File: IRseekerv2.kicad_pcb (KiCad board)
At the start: 2 copper layers, 100 x 100 mm, 39 parts, among them J1 Conn_01x01_Female, J10 Conn_01x01_Female, J11 Conn_01x01_Female, J12 Conn_01x01_Female, J13 RESET, J14 COMM, J15 SEL_VOLTAGE, J16 G, J17 G, J18 G, J19 G, J2 Conn_01x01_Female, J20 COMM, J21 Conn_01x01_Female, J22 Conn_01x01_Female, J23 Conn_01x01_Female, J24 Conn_01x01_Female, J3 Conn_01x01_Female, J4 Conn_01x01_Female, J5 Conn_01x01_Female, J6 Conn_01x01_Female, J7 Conn_01x01_Female, J8 Conn_01x01_Female, J9 Conn_01x01_Female, U1 WeAct-STM32G431CoreBoard, U10 TSSP58038, U11 TSSP58038, U12 TSSP58038, U13 TSSP58038, U14 TSSP58038, U15 TSSP58038, U16 TSSP58038, U2 CD4072B, U4 CD4072B, U5 TSSP58038, U6 TSSP58038, U7 TSSP58038, U8 TSSP58038, U9 TSSP58038

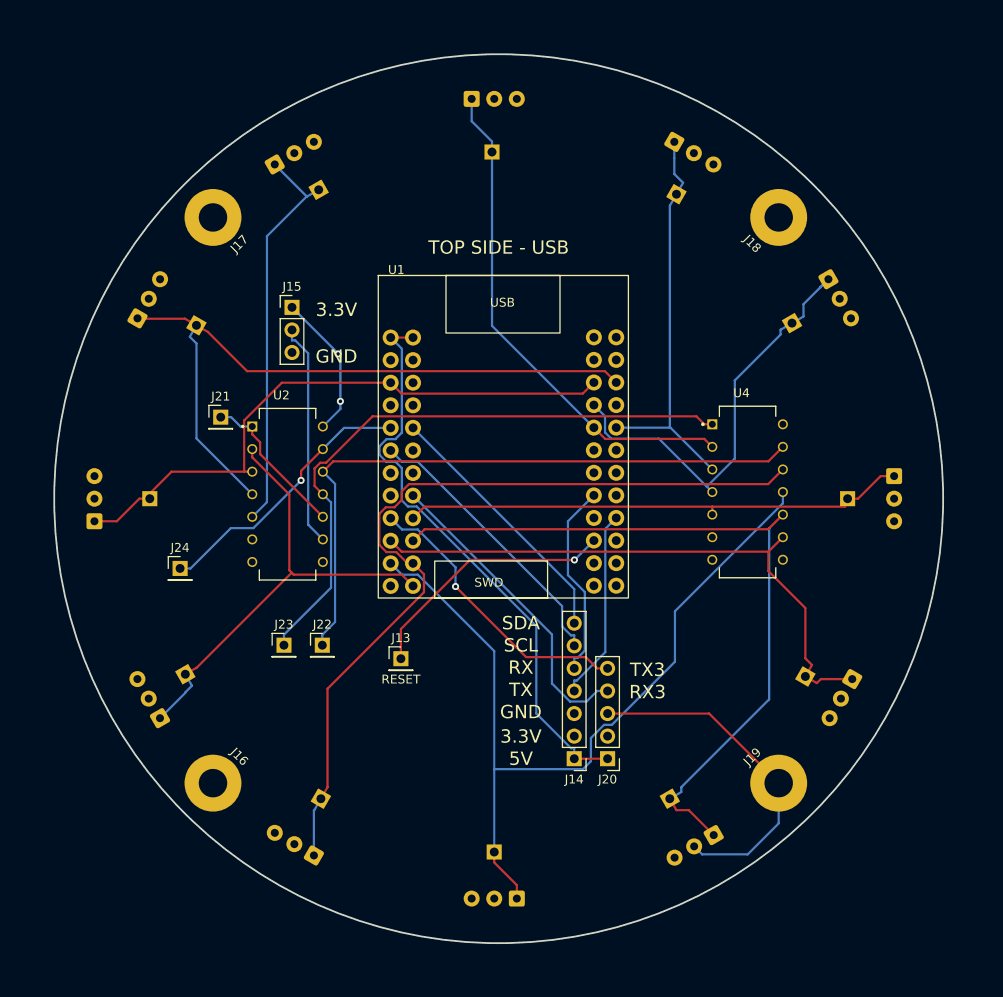
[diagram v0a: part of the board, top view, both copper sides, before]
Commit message: reworked to put STM32G431CBU6 on board
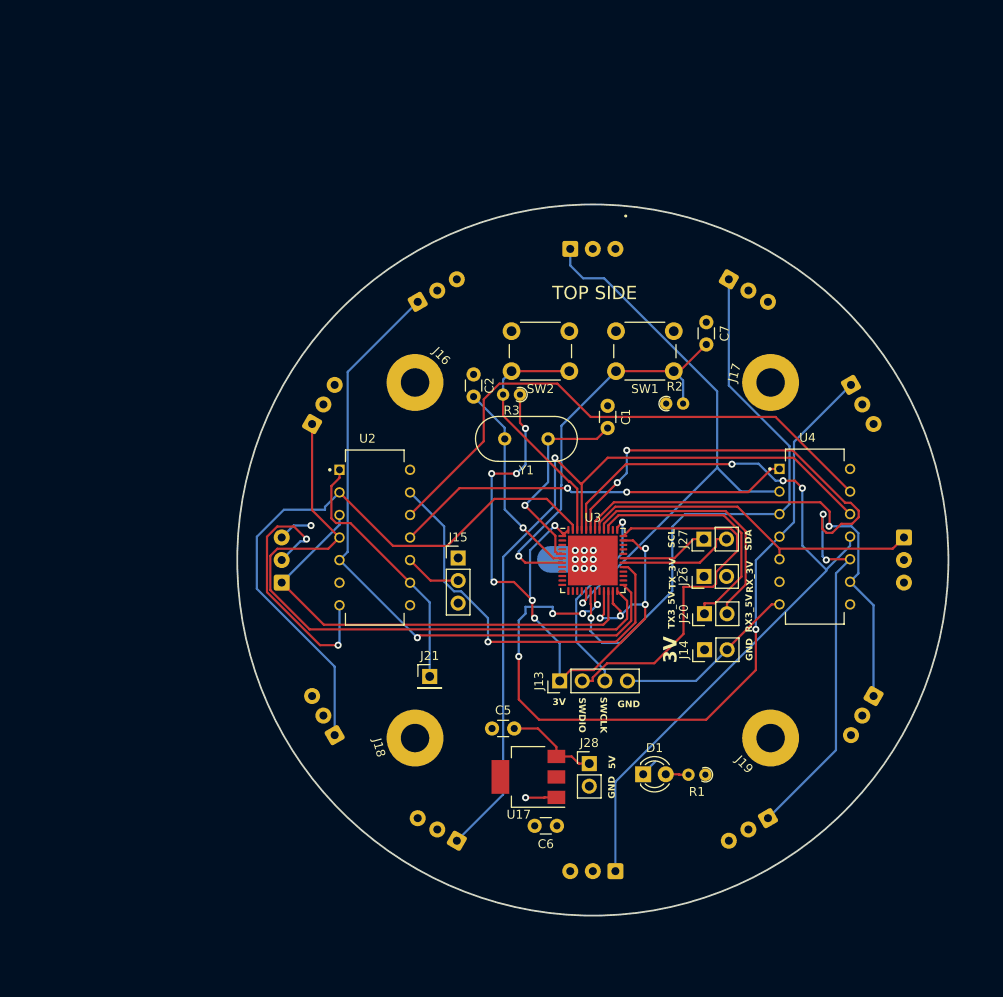
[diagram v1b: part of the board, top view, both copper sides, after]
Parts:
- removed J1, J10, J11, J12, J2, J22, J23, J24, J3, J4, J5, J6, J7, J8, J9: Conn_01x01_Female, Connector_PinHeader_2.54mm:PinHeader_1x01_P2.54mm_Vertical
- removed U1: WeAct-STM32G431CoreBoard, bluepill:WeAct-STM32G431CoreBoard_MCU_Module
- added C1: 10pF, Capacitor_THT:C_Disc_D3.0mm_W1.6mm_P2.50mm, F.Cu at (105.8, 83.1)
- added C2: 10pF, Capacitor_THT:C_Disc_D3.0mm_W1.6mm_P2.50mm, F.Cu at (90.7, 79.5)
- added C5: 10uF, Capacitor_THT:C_Disc_D3.0mm_W1.6mm_P2.50mm, F.Cu at (92.8, 119.3)
- added C6: 10uF, Capacitor_THT:C_Disc_D3.0mm_W1.6mm_P2.50mm, F.Cu at (100.0, 130.3)
- added C7: 100nF, Capacitor_THT:C_Disc_D3.0mm_W1.6mm_P2.50mm, F.Cu at (116.9, 73.7)
- added D1: LED, LED_THT:LED_D3.0mm, F.Cu at (109.8, 124.5)
- added J26: Conn_01x02_Pin, Connector_PinHeader_2.54mm:PinHeader_1x02_P2.54mm_Vertical, F.Cu at (116.6, 102.2)
- added J27: Conn_01x02_Pin, Connector_PinHeader_2.54mm:PinHeader_1x02_P2.54mm_Vertical, F.Cu at (116.6, 98.0)
- added J28: Conn_01x02_Pin, Connector_PinHeader_2.54mm:PinHeader_1x02_P2.54mm_Vertical, F.Cu at (103.7, 123.3)
- added R1: 330R, Resistor_THT:R_Axial_DIN0204_L3.6mm_D1.6mm_P1.90mm_Vertical, F.Cu at (116.8, 124.5)
- added R2: 10kR, Resistor_THT:R_Axial_DIN0204_L3.6mm_D1.6mm_P1.90mm_Vertical, F.Cu at (112.3, 82.8)
- added R3: 10kR, Resistor_THT:R_Axial_DIN0204_L3.6mm_D1.6mm_P1.90mm_Vertical, F.Cu at (95.9, 81.8)
- added SW1: SW_Push, Button_Switch_THT:SW_PUSH_6mm, F.Cu at (113.2, 79.2)
- added SW2: SW_Push, Button_Switch_THT:SW_PUSH_6mm, F.Cu at (101.4, 79.2)
- added U17: AMS1117-3.3, Package_TO_SOT_SMD:SOT-223-3_TabPin2, F.Cu at (96.8, 124.8)
- added U3: STM32G431CBUx, Package_DFN_QFN:QFN-48-1EP_7x7mm_P0.5mm_EP5.6x5.6mm, F.Cu at (104.1, 100.5)
- added Y1: Crystal, Crystal:Crystal_HC49-4H_Vertical, F.Cu at (99.1, 86.8)
- J13: value RESET -> Conn_01x04_Pin; footprint Connector_PinHeader_2.54mm:PinHeader_1x01_P2.54mm_Vertical -> Connector_PinHeader_2.54mm:PinHeader_1x04_P2.54mm_Vertical
- J14: value COMM -> Conn_01x02_Pin; footprint Connector_PinHeader_2.54mm:PinHeader_1x07_P2.54mm_Vertical -> Connector_PinHeader_2.54mm:PinHeader_1x02_P2.54mm_Vertical
- J20: value COMM -> Conn_01x02_Pin; footprint Connector_PinHeader_2.54mm:PinHeader_1x05_P2.54mm_Vertical -> Connector_PinHeader_2.54mm:PinHeader_1x02_P2.54mm_Vertical
- U10, U12, U14, U15, U5, U7: value TSSP58038 -> TSSP4038; footprint OptoDevice:Vishay_MINICAST-3Pin -> Vishay:Vishay_MINICAST-3Pin
- U11, U13, U16, U6, U8, U9: value TSSP58038 -> TSSP4038; footprint Library:Vishay_MINICAST-3PinMarek -> Vishay:Vishay_MINICAST-3Pin
- U2: value CD4072B -> CD4012; footprint CD4072B:DIP794W45P254L1969H508Q14 -> CD70xx:DIP794W45P254L1969H508Q14
- U4: value CD4072B -> CD4012B; footprint CD4072B:DIP794W45P254L1969H508Q14 -> CD70xx:DIP794W45P254L1969H508Q14
- moved J18 71.4 mm to (84.1, 120.4), turned to 105 degrees
- moved J17 65.4 mm to (124.1, 80.4), turned to 75 degrees
- moved J16 50.5 mm to (84.1, 80.4)
- moved J21 37.5 mm to (85.7, 113.5)
- moved J15 33.8 mm to (88.9, 100.2)
- moved U16 23.3 mm to (86.6, 70.1)
- moved U15 23.0 mm to (73.8, 82.9)
- moved U5 21.7 mm to (104.1, 65.4)
- moved U14 21.5 mm to (69.1, 100.4)
- moved U13 20.6 mm to (73.8, 117.9)
- moved J20 19.6 mm to (116.6, 106.4), turned to 90 degrees
- moved J14 19.1 mm to (116.7, 110.5), turned to 90 degrees
- moved J13 18.0 mm to (100.4, 114.0), turned to 90 degrees
- moved U6 17.3 mm to (121.6, 70.1)
- moved U7 14.6 mm to (134.4, 82.9)
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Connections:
- J13 pad 1: Net-(J13-Pad1) -> +3.3V
- J14 pad 1: +5V -> +3.3V
- J14 pad 2: +3.3V -> GND
- J15 pad 2: Net-(J15-Pad2) -> Net-(J15-Pin_2)
- J20 pad 1: +5V -> TX3_5V
- J20 pad 2: +3.3V -> RX3_5V
- J21 pad 1: Net-(U2-PadP1) -> Net-(J21-Pin_1)
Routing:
- net +3.3V: track 16.5 -> 91.9 mm, vias 2 -> 12
- net Net-(U2-PadP12): track 73.6 -> 0.00 mm
- net Net-(U2-PadP11): track 70.4 -> 0.00 mm
- net Net-(J22-Pin_1): track 0.00 -> 63.4 mm
- net +5V: track 66.3 -> 10.7 mm
- net RESET: track 0.00 -> 46.0 mm, vias 0 -> 1
- net Net-(J23-Pin_1): track 0.00 -> 45.1 mm, vias 0 -> 2
- net SWDIO: track 0.00 -> 42.8 mm
- net I3: track 48.3 -> 88.1 mm, vias 0 -> 5
- net TX3: track 35.2 -> 0.00 mm
- net RX3: track 32.7 -> 0.00 mm, vias 1 -> 0
- net Net-(J13-Pad1): track 29.2 -> 0.00 mm, vias 1 -> 0
- net Net-(J21-Pin_1): track 0.00 -> 29.2 mm
- net I12: track 45.2 -> 74.3 mm, vias 0 -> 1
- net RX3_5V: track 0.00 -> 28.3 mm
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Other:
- board size 100 x 100 mm -> 80 x 80 mm
- board text added: "3V"
- board text added: "RX3_5V"
- board text added: "RX_3V"
- board text added: "SWCLK"
- board text added: "SWDIO"
- board text added: "TOP SIDE"
- board text added: "TX3_5V"
- board text added: "TX_3V"
- board text removed: "3.3V"
- board text removed: "RX"
- board text removed: "RX3"
- board text removed: "TOP SIDE - USB"
- board text removed: "TX"
- board text removed: "TX3"

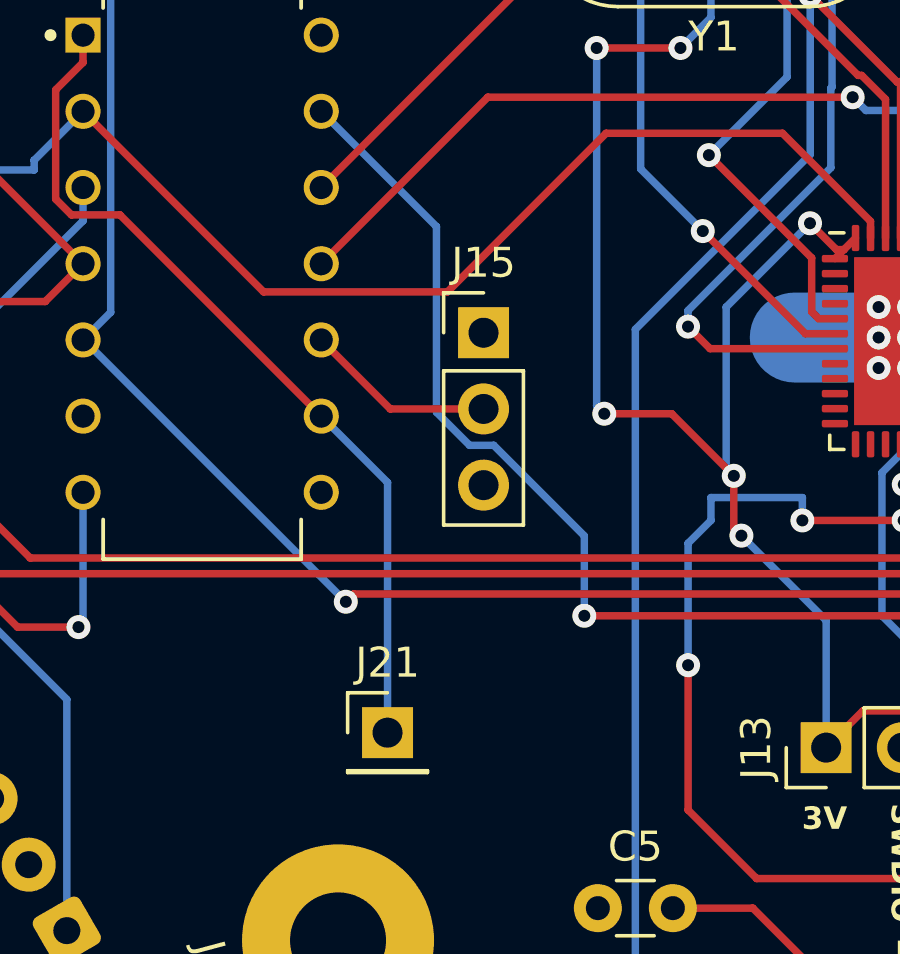
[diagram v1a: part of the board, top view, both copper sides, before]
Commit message: Writen more info in README and removed output jumper in PCB
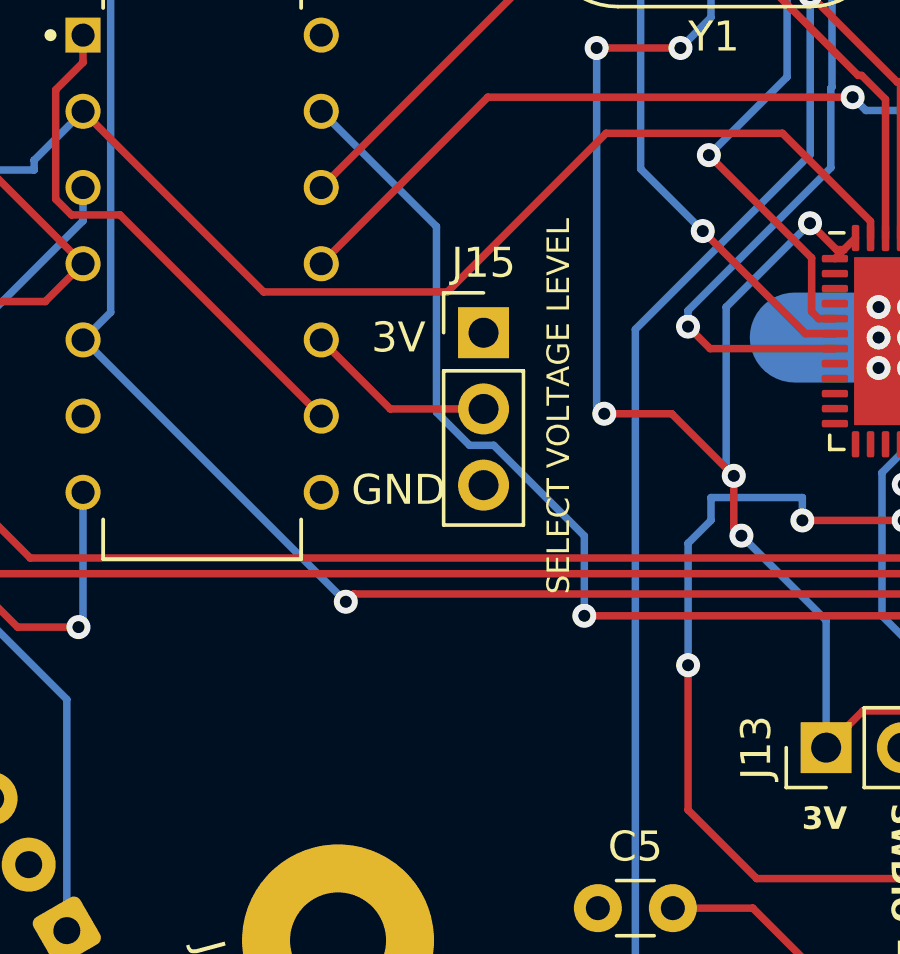
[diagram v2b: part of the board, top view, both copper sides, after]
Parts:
- removed J21: Conn_01x01_Female, Connector_PinHeader_2.54mm:PinHeader_1x01_P2.54mm_Vertical
- J15: value SEL_VOLTAGE -> SELECT VOLTAGE LEVEL
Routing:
- net Net-(J21-Pin_1): track 29.2 -> 17.7 mm
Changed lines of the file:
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@@
       (net 5 "+3.3V") (pinfunction "VDD") (pintype "power_in") (solder_mask_margin 0.102))
   )
-  (footprint "Connector_PinHeader_2.54mm:PinHeader_1x01_P2.54mm_Vertical" (layer "F.Cu")
-    (at 85.74 113.5)
-    (descr "Through hole straight pin header, 1x01, 2.54mm pitch, single row")
-    (tags "Through hole pin header THT 1x01 2.54mm single row")
-    (property "Sheetfile" "IRseekerv2.kicad_sch")
-    (property "Sheetname" "")
-    (property "ki_description" "Generic connector, single row, 01x01, script generated (kicad-library-utils/schlib/autogen/connector/)")
-    (property "ki_keywords" "connector")
-    (attr through_hole)
-    (fp_text reference "J21" (at 0 -2.33) (layer "F.SilkS")
-        (effects (font (size 1 1) (thickness 0.15)))
-    )
-    (fp_text value "Conn_01x01_Female" (at 0 2.33) (layer "F.Fab")
-        (effects (font (size 1 1) (thickness 0.15)))
-    )
-    (fp_text user "${REFERENCE}" (at 0 0 90) (layer "F.Fab")
-        (effects (font (size 1 1) (thickness 0.15)))
-    )
-    (fp_line (start -1.33 -1.33) (end 0 -1.33)
-      (stroke (width 0.12) (type solid)) (layer "F.SilkS"))
-    (fp_line (start -1.33 0) (end -1.33 -1.33)
-      (stroke (width 0.12) (type solid)) (layer "F.SilkS"))
-    (fp_line (start -1.33 1.27) (end -1.33 1.33)
-      (stroke (width 0.12) (type solid)) (layer "F.SilkS"))
-    (fp_line (start -1.33 1.27) (end 1.33 1.27)
-      (stroke (width 0.12) (type solid)) (layer "F.SilkS"))
-    (fp_line (start -1.33 1.33) (end 1.33 1.33)
-      (stroke (width 0.12) (type solid)) (layer "F.SilkS"))
-    (fp_line (start 1.33 1.27) (end 1.33 1.33)
-      (stroke (width 0.12) (type solid)) (layer "F.SilkS"))
-    (fp_line (start -1.8 -1.8) (end -1.8 1.8)
-      (stroke (width 0.05) (type solid)) (layer "F.CrtYd"))
-    (fp_line (start -1.8 1.8) (end 1.8 1.8)
-      (stroke (width 0.05) (type solid)) (layer "F.CrtYd"))
-    (fp_line (start 1.8 -1.8) (end -1.8 -1.8)
-      (stroke (width 0.05) (type solid)) (layer "F.CrtYd"))
-    (fp_line (start 1.8 1.8) (end 1.8 -1.8)
-      (stroke (width 0.05) (type solid)) (layer "F.CrtYd"))
-    (fp_line (start -1.27 -0.635) (end -0.635 -1.27)
-      (stroke (width 0.1) (type solid)) (layer "F.Fab"))
-    (fp_line (start -1.27 1.27) (end -1.27 -0.635)
-      (stroke (width 0.1) (type solid)) (layer "F.Fab"))
-    (fp_line (start -0.635 -1.27) (end 1.27 -1.27)
-      (stroke (width 0.1) (type solid)) (layer "F.Fab"))
-    (fp_line (start 1.27 -1.27) (end 1.27 1.27)
-      (stroke (width 0.1) (type solid)) (layer "F.Fab"))
-    (fp_line (start 1.27 1.27) (end -1.27 1.27)
-      (stroke (width 0.1) (type solid)) (layer "F.Fab"))
-    (pad "1" thru_hole rect (at 0 0) (size 1.7 1.7) (drill 1) (layers "*.Cu" "*.Mask")
-      (net 8 "Net-(J21-Pin_1)") (pinfunction "Pin_1") (pintype "passive"))
-    (model "${KICAD6_3DMODEL_DIR}/Connector_PinHeader_2.54mm.3dshapes/PinHeader_1x01_P2.54mm_Vertical.wrl"
-      (offset (xyz 0 0 0))
-      (scale (xyz 1 1 1))
-      (rotate (xyz 0 0 0))
-    )
-  )
   (footprint "Connector_PinHeader_2.54mm:PinHeader_1x02_P2.54mm_Vertical" (layer "F.Cu")
     (at 103.69 123.3)
@@
         (effects (font (size 1 1) (thickness 0.15)))
     )
-    (fp_text value "SEL_VOLTAGE" (at -4.75 7.83) (layer "F.Fab")
-        (effects (font (size 1 1) (thickness 0.15)))
+    (fp_text value "SELECT VOLTAGE LEVEL" (at 2.5 2.446 90) (layer "F.SilkS")
+        (effects (font (size 0.75 0.75) (thickness 0.15)))
     )
     (fp_text user "${REFERENCE}" (at 0 2.54 90) (layer "F.Fab")
@@
     (effects (font (size 0.75 0.75) (thickness 0.1875) bold) (justify left bottom))
   )
+  (gr_text "GND" (at 86.106 105.41) (layer "F.SilkS")
+    (effects (font (size 1 1) (thickness 0.15)))
+  )
   (gr_text "RX3_5V" (at 122.086 108.544 90) (layer "F.SilkS")
     (effects (font (size 0.75 0.75) (thickness 0.1875) bold) (justify left bottom))
@@
     (effects (font (size 0.75 0.75) (thickness 0.1875) bold) (justify left bottom))
   )
+  (gr_text "3V" (at 86.106 100.33) (layer "F.SilkS")
+    (effects (font (size 1 1) (thickness 0.15)))
+  )
   (gr_text "3V" (at 113.686 111.994 90) (layer "F.SilkS")
     (effects (font (size 1.5 1.5) (thickness 0.3) bold) (justify left bottom))
@@
   (segment (start 75.59 90.25) (end 75.59 91.1619) (width 0.25) (layer "F.Cu") (net 8))
   (segment (start 74.6781 95.7161) (end 74.6781 92.0738) (width 0.25) (layer "F.Cu") (net 8))
-  (segment (start 85.74 105.16) (end 83.53 102.95) (width 0.25) (layer "B.Cu") (net 8))
-  (segment (start 85.74 113.5) (end 85.74 105.16) (width 0.25) (layer "B.Cu") (net 8))
   (segment (start 112.295 124.5) (end 113.7731 124.5) (width 0.25) (layer "F.Cu") (net 9))
   (segment (start 114.85 124.55) (end 113.8231 124.55) (width 0.25) (layer "F.Cu") (net 9))
@@
     )
   )
-  (zone (net 8) (net_name "Net-(J21-Pin_1)") (layer "B.Cu") (name "$teardrop_padvia$") (hatch edge 0.5)
-    (priority 30031)
-    (attr (teardrop (type padvia)))
-    (connect_pads yes (clearance 0))
-    (min_thickness 0.0254) (filled_areas_thickness no)
-    (fill yes (thermal_gap 0.5) (thermal_bridge_width 0.5) (island_removal_mode 1) (island_area_min 10))
-    (polygon
-      (pts
-        (xy 84.268926 103.865702)
-        (xy 84.445702 103.688926)
-        (xy 84.07047 102.72613)
-        (xy 83.529293 102.949293)
-        (xy 83.30613 103.49047)
-      )
-    )
-  )
   (zone (net 2) (net_name "Net-(U3-PF1)") (layer "B.Cu") (name "$teardrop_padvia$") (hatch edge 0.5)
     (priority 30019)
@@
       )
     )
-  )
-  (zone (net 8) (net_name "Net-(J21-Pin_1)") (layer "B.Cu") (name "$teardrop_padvia$") (hatch edge 0.5)
-    (priority 30014)
-    (attr (teardrop (type padvia)))
-    (connect_pads yes (clearance 0))
-    (min_thickness 0.0254) (filled_areas_thickness no)
-    (fill yes (thermal_gap 0.5) (thermal_bridge_width 0.5) (island_removal_mode 1) (island_area_min 10))
-    (polygon
-      (pts
-        (xy 85.865 111.8)
-        (xy 85.615 111.8)
-        (xy 84.89 112.65)
-        (xy 85.74 113.501)
-        (xy 86.59 112.65)
-      )
-    )

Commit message: I2C pullup resistors
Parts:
- added R4: 4.7kR, Resistor_THT:R_Axial_DIN0204_L3.6mm_D1.6mm_P2.54mm_Vertical, F.Cu at (79.2, 111.4)
- added R5: 4.7kR, Resistor_THT:R_Axial_DIN0204_L3.6mm_D1.6mm_P2.54mm_Vertical, F.Cu at (81.7, 114.8)
- J15: value SELECT VOLTAGE LEVEL -> SEL_VOLTAGE
- moved J27 33.9 mm to (86.6, 113.8)
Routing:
- net SCL: track 9.95 -> 58.1 mm, vias 0 -> 2
- net SDA: track 13.2 -> 54.9 mm, vias 0 -> 4
- net I12: track 74.3 -> 74.9 mm
